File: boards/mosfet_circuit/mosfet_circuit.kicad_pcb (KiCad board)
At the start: 2 copper layers, 56.3 x 41 mm, 14 parts, among them J1 Vin, J2 control_in, J4 LED, Q1 BUZ11, Q2 IRF4905

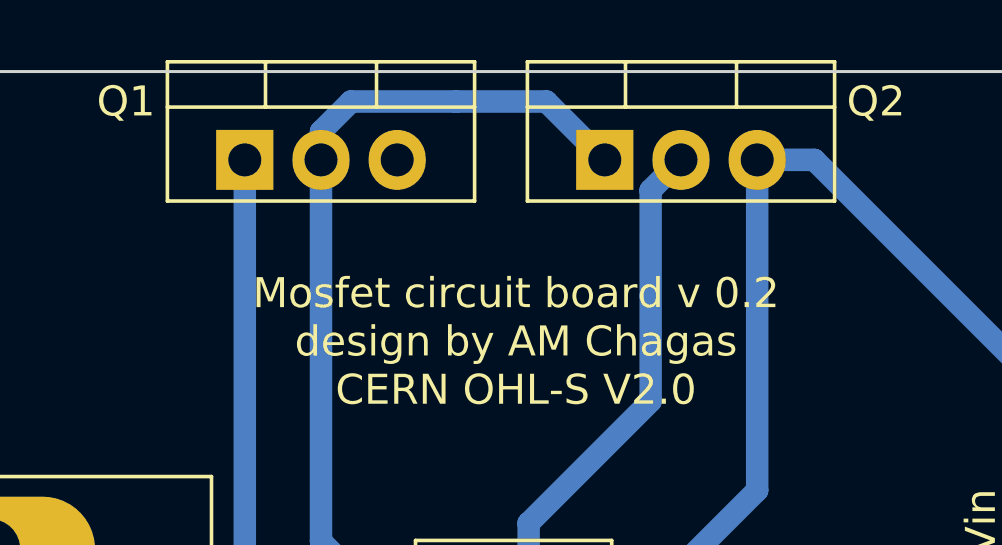
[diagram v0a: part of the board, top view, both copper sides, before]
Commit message: update mosfet id on board
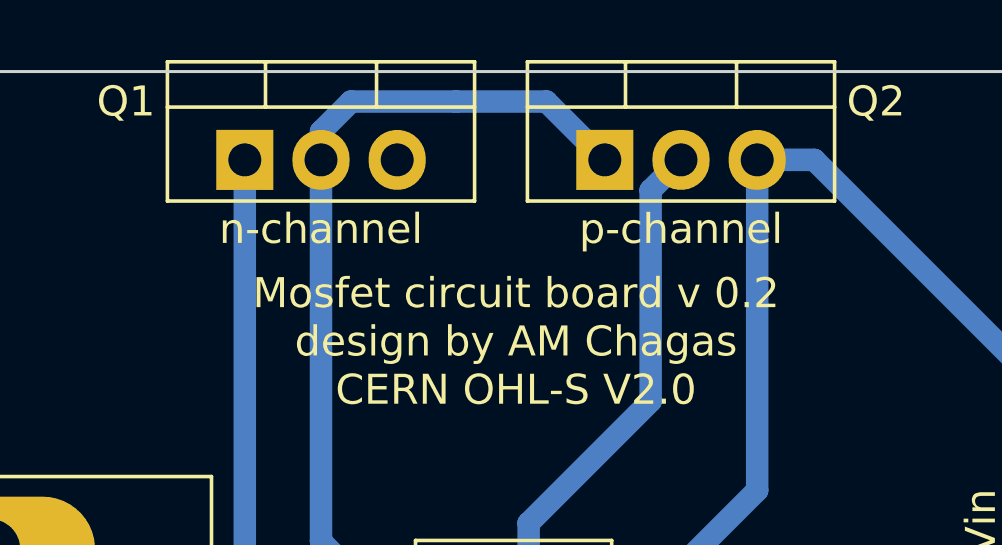
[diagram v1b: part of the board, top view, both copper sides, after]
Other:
- board text added: "n-channel"
- board text added: "p-channel"
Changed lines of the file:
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@@
     (effects (font (size 1 1) (thickness 0.15)))
+  )
+  (gr_text "n-channel\n" (at 177.5 70.25) (layer "F.SilkS")
+    (effects (font (size 1 1) (thickness 0.2)))
+  )
+  (gr_text "p-channel\n" (at 189.5 70.25) (layer "F.SilkS")
+    (effects (font (size 1 1) (thickness 0.2)))
   )
   (gr_text "+" (at 201 82.5) (layer "F.SilkS")
